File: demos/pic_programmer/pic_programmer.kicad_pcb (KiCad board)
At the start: 2 copper layers, 160 x 99.1 mm, 63 parts, among them J1 DB9-FEMAL, P1 CONN_2, P101 CONN_1, P102 CONN_1, P103 CONN_1, P104 CONN_1, P105 CONN_1, P106 CONN_1, P2 SUPP28, P3 SUPP40, Q1 BC237, Q2 BC307, Q3 BC307, U1 24Cxx, U2 74HC125, U3 7805, U4 LT1373, U5 PIC_18_PINS, U6 PIC_8_PINS

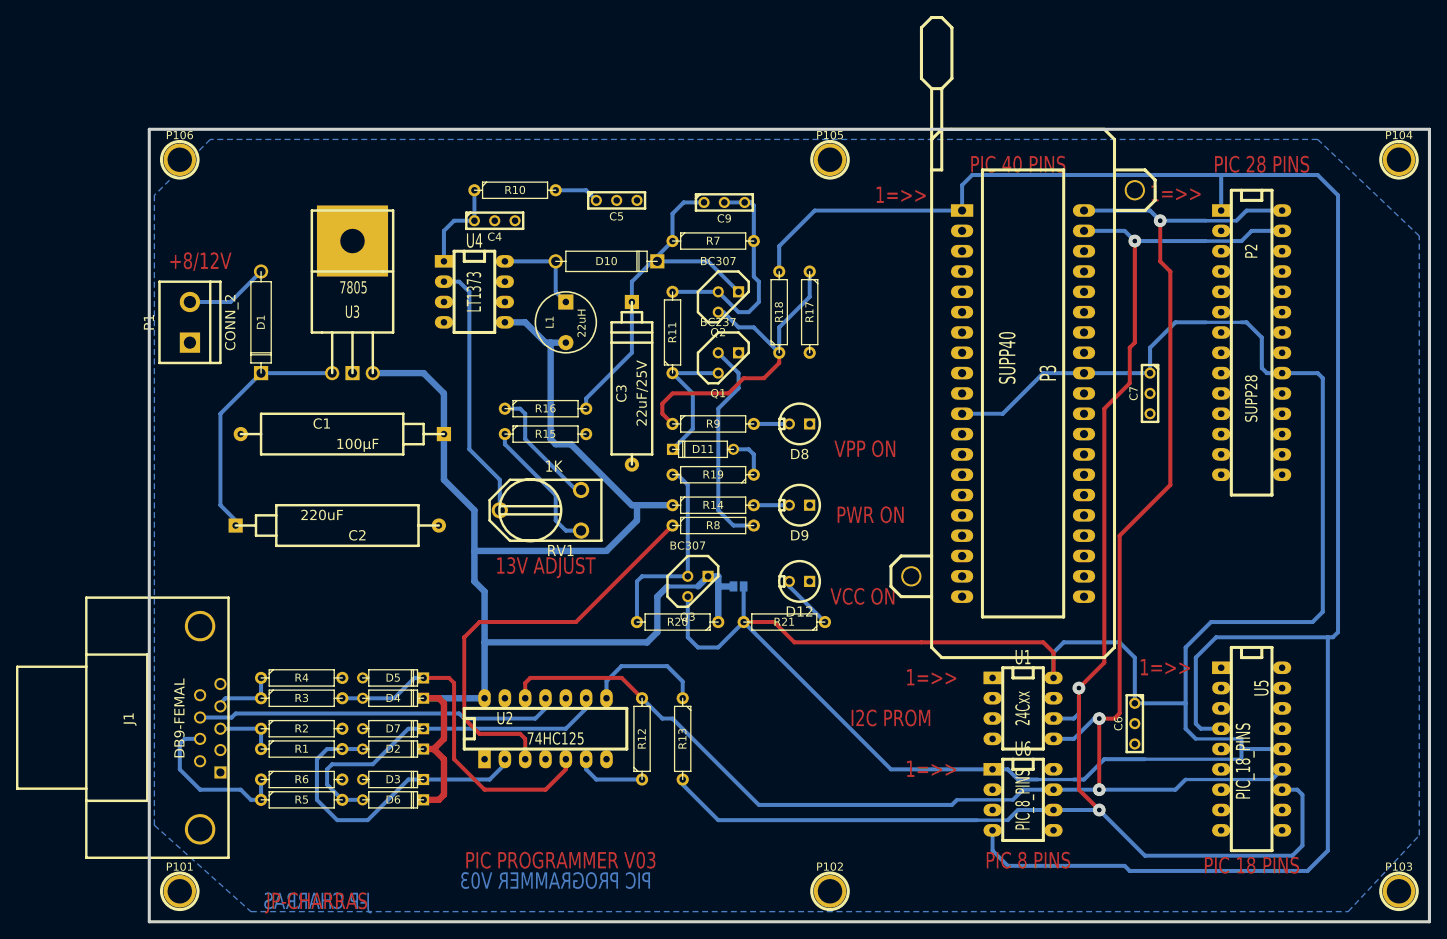
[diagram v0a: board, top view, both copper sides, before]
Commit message: Update demo to use latest libraries.
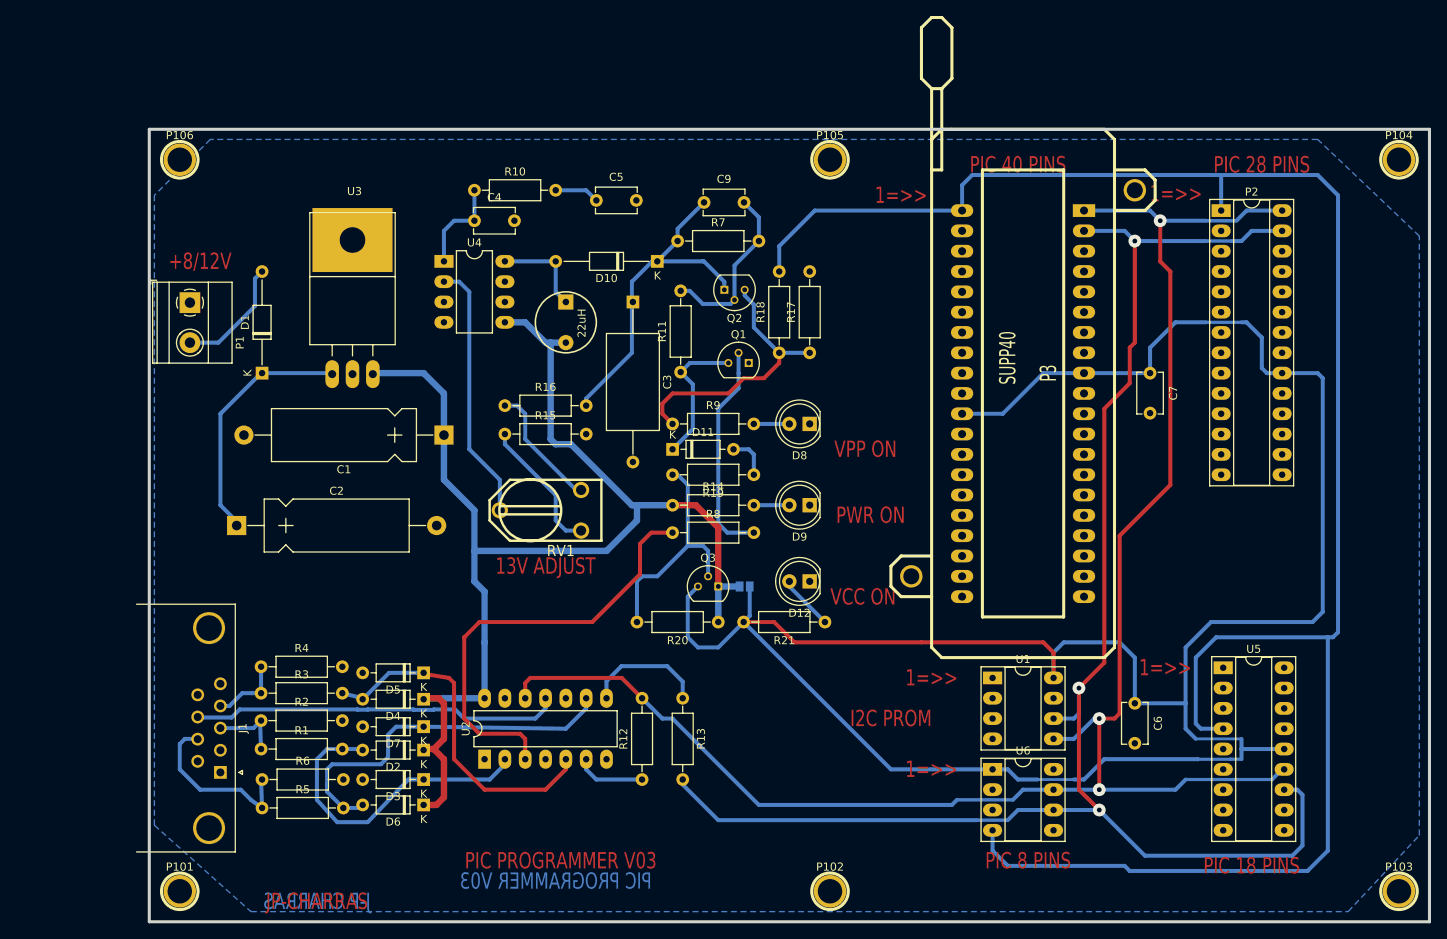
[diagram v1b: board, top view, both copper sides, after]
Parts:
- C1, C2: footprint Discret:CP10 -> Capacitors_THT:CP_Axial_L18.0mm_D6.5mm_P25.00mm_Horizontal
- C3: footprint Discret:CP8 -> Capacitors_THT:C_Axial_L12.0mm_D6.5mm_P20.00mm_Horizontal
- C4, C5, C6, C7, C9: footprint Discret:C1-1 -> C_Disc_D5.1mm_W3.2mm_P5.00mm
- D1, D10: footprint Discret:D5 -> Diode_THT:D_DO-35_SOD27_P12.70mm_Horizontal
- D11, D2, D3, D4, D5, D6, D7: footprint Discret:D3 -> Diode_THT:D_DO-35_SOD27_P7.62mm_Horizontal
- D12, D8, D9: footprint Discret:LEDV -> footprints:LED_D5.0mm
- J1: footprint connect:DB9FC -> Connector_Dsub:DSUB-9_Female_Horizontal_P2.77x2.84mm_EdgePinOffset7.70mm_Housed_MountingHolesOffset9.12mm
- L1: footprint inductors:INDUCTOR_V -> footprints:INDUCTOR_V
- P1: footprint connect:bornier2 -> TerminalBlock_Phoenix:TerminalBlock_Phoenix_MKDS-1,5-2_1x02_P5.00mm_Horizontal
- P2: footprint dip_sockets:DIP-28__300_ELL -> Package_DIP:DIP-28_W7.62mm_Socket_LongPads
- P3: footprint sockets:40tex-Ell600 -> 40tex-Ell600
- Q1, Q2, Q3: footprint Discret:TO92 -> footprints:TO-92_BC237_307
- R1, R10, R11, R12, R13, R14, R15, R16, R17, R18, R19, R2, R20, R21, R3, R4, R5, R6, R7, R8, R9: footprint Discret:R4 -> Resistors_THT:R_Axial_DIN0207_L6.3mm_D2.5mm_P10.16mm_Horizontal
- RV1: footprint Discret:RV2X4 -> footprints:RV2X4
- U1, U6: footprint dip_sockets:DIP-8__300_ELL -> Package_DIP:DIP-8_W7.62mm_Socket_LongPads
- U2: footprint dip_sockets:DIP-14__300_ELL -> Package_DIP:DIP-14_W7.62mm_LongPads
- U3: footprint Discret:LM78XX -> footprints:TO-220_LM78xx
- U4: footprint dip_sockets:DIP-8__300_ELL -> Package_DIP:DIP-8_W7.62mm_LongPads
- U5: footprint dip_sockets:DIP-18__300_ELL -> Package_DIP:DIP-18_W7.62mm_Socket_LongPads
- moved P2 16.9 mm to (207.6, 50.8), turned to 0 degrees
- moved C1 12.7 mm to (110.5, 78.9)
- moved C2 12.6 mm to (84.6, 90.2)
- moved U5 10.8 mm to (207.9, 108.0), turned to 0 degrees
- moved C3 10.2 mm to (134.1, 62.2)
- moved U2 8.52 mm to (115.6, 119.4), turned to 90 degrees
- moved D1 6.35 mm to (87.8, 71.1), turned to 90 degrees
- moved D10 6.35 mm to (137.2, 57.1), turned to 180 degrees
- moved J1 5.61 mm to (82.5, 121.0), turned to 270 degrees
- moved U1 5.39 mm to (179.1, 109.2), turned to 0 degrees
- moved U4 5.39 mm to (110.5, 57.1), turned to 0 degrees
- moved U6 5.39 mm to (179.1, 120.7), turned to 0 degrees
- moved R4 5.27 mm to (87.6, 107.8)
- moved R2 5.18 mm to (87.6, 114.6)
- moved R8 5.16 mm to (139.1, 91.1)
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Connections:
- J1 pad 1: (no net) -> Net-(J1-Pad1)
- J1 pad 2: (no net) -> Net-(J1-Pad2)
- J1 pad 6: (no net) -> Net-(J1-Pad6)
- J1 pad 9: (no net) -> Net-(J1-Pad9)
- P101 pad 1: (no net) -> Net-(P101-Pad1)
- P102 pad 1: (no net) -> Net-(P102-Pad1)
- P103 pad 1: (no net) -> Net-(P103-Pad1)
- P104 pad 1: (no net) -> Net-(P104-Pad1)
- P105 pad 1: (no net) -> Net-(P105-Pad1)
- P106 pad 1: (no net) -> Net-(P106-Pad1)
- P2 pad 10: (no net) -> Net-(P2-Pad10)
- P2 pad 11: (no net) -> Net-(P2-Pad11)
- P2 pad 12: (no net) -> Net-(P2-Pad12)
- P2 pad 13: (no net) -> Net-(P2-Pad13)
- P2 pad 14: (no net) -> Net-(P2-Pad14)
- P2 pad 15: (no net) -> Net-(P2-Pad15)
- P2 pad 16: (no net) -> Net-(P2-Pad16)
- P2 pad 17: (no net) -> Net-(P2-Pad17)
- P2 pad 18: (no net) -> Net-(P2-Pad18)
- P2 pad 2: (no net) -> Net-(P2-Pad2)
- P2 pad 21: (no net) -> Net-(P2-Pad21)
- P2 pad 22: (no net) -> Net-(P2-Pad22)
- P2 pad 23: (no net) -> Net-(P2-Pad23)
- P2 pad 24: (no net) -> Net-(P2-Pad24)
- P2 pad 25: (no net) -> Net-(P2-Pad25)
- P2 pad 26: (no net) -> Net-(P2-Pad26)
- P2 pad 3: (no net) -> Net-(P2-Pad3)
- P2 pad 4: (no net) -> Net-(P2-Pad4)
- P2 pad 5: (no net) -> Net-(P2-Pad5)
- P2 pad 6: (no net) -> Net-(P2-Pad6)
- P2 pad 7: (no net) -> Net-(P2-Pad7)
- P2 pad 9: (no net) -> Net-(P2-Pad9)
- P3 pad 10: (no net) -> Net-(P3-Pad10)
- P3 pad 13: (no net) -> Net-(P3-Pad13)
- P3 pad 14: (no net) -> Net-(P3-Pad14)
- P3 pad 15: (no net) -> Net-(P3-Pad15)
- P3 pad 16: (no net) -> Net-(P3-Pad16)
- P3 pad 17: (no net) -> Net-(P3-Pad17)
- P3 pad 18: (no net) -> Net-(P3-Pad18)
- P3 pad 19: (no net) -> Net-(P3-Pad19)
- P3 pad 2: (no net) -> Net-(P3-Pad2)
- P3 pad 20: (no net) -> Net-(P3-Pad20)
- P3 pad 21: (no net) -> Net-(P3-Pad21)
- P3 pad 22: (no net) -> Net-(P3-Pad22)
- P3 pad 23: (no net) -> Net-(P3-Pad23)
- P3 pad 24: (no net) -> Net-(P3-Pad24)
- P3 pad 25: (no net) -> Net-(P3-Pad25)
- P3 pad 26: (no net) -> Net-(P3-Pad26)
- P3 pad 27: (no net) -> Net-(P3-Pad27)
- P3 pad 28: (no net) -> Net-(P3-Pad28)
- P3 pad 29: (no net) -> Net-(P3-Pad29)
- P3 pad 3: (no net) -> Net-(P3-Pad3)
- P3 pad 30: (no net) -> Net-(P3-Pad30)
- P3 pad 33: (no net) -> Net-(P3-Pad33)
- P3 pad 34: (no net) -> Net-(P3-Pad34)
- P3 pad 35: (no net) -> Net-(P3-Pad35)
- P3 pad 36: (no net) -> Net-(P3-Pad36)
- P3 pad 37: (no net) -> Net-(P3-Pad37)
- P3 pad 38: (no net) -> Net-(P3-Pad38)
- P3 pad 4: (no net) -> Net-(P3-Pad4)
- P3 pad 5: (no net) -> Net-(P3-Pad5)
- P3 pad 6: (no net) -> Net-(P3-Pad6)
- P3 pad 7: (no net) -> Net-(P3-Pad7)
- P3 pad 9: (no net) -> Net-(P3-Pad9)
- U1 pad 7: (no net) -> Net-(U1-Pad7)
- U4 pad 3: (no net) -> Net-(U4-Pad3)
- U4 pad 4: (no net) -> Net-(U4-Pad4)
- U5 pad 1: (no net) -> Net-(U5-Pad1)
- U5 pad 10: (no net) -> Net-(U5-Pad10)
- U5 pad 11: (no net) -> Net-(U5-Pad11)
- U5 pad 15: (no net) -> Net-(U5-Pad15)
- U5 pad 16: (no net) -> Net-(U5-Pad16)
- U5 pad 17: (no net) -> Net-(U5-Pad17)
- U5 pad 18: (no net) -> Net-(U5-Pad18)
- U5 pad 2: (no net) -> Net-(U5-Pad2)
- U5 pad 3: (no net) -> Net-(U5-Pad3)
- U5 pad 6: (no net) -> Net-(U5-Pad6)
- U5 pad 7: (no net) -> Net-(U5-Pad7)
- U5 pad 8: (no net) -> Net-(U5-Pad8)
- U5 pad 9: (no net) -> Net-(U5-Pad9)
- U6 pad 2: (no net) -> Net-(U6-Pad2)
- U6 pad 3: (no net) -> Net-(U6-Pad3)
- U6 pad 5: (no net) -> Net-(U6-Pad5)
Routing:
- net VCC: track 183.3 -> 162.1 mm
- net Net-(Q2-Pad3): track 42.5 -> 34.5 mm
- net Net-(C9-Pad2): track 28.5 -> 21.8 mm
- net Net-(D1-Pad2): track 10.5 -> 14.7 mm
- net Net-(Q3-Pad2): track 25.6 -> 29.3 mm
- net VPP: track 45.5 -> 42.3 mm
- net Net-(D6-Pad2): track 44.0 -> 46.8 mm
- net /pic_sockets/VCC_PIC: track 290.3 -> 292.4 mm
- net Net-(R8-Pad1): track 53.2 -> 55.1 mm
- net /PC-CLOCK-OUT: track 20.3 -> 21.7 mm
- net /TXD: track 7.62 -> 9.03 mm
- net /DTR: track 8.26 -> 9.04 mm

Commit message: Update demo
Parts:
- C4, C5, C6, C7, C9: footprint C_Disc_D5.1mm_W3.2mm_P5.00mm -> Capacitor_THT:C_Disc_D5.1mm_W3.2mm_P5.00mm
- P3: footprint 40tex-Ell600 -> footprints:40tex-Ell600
- R1, R10, R11, R12, R13, R14, R15, R16, R17, R18, R19, R2, R20, R21, R3, R4, R5, R6, R7, R8, R9: footprint Resistors_THT:R_Axial_DIN0207_L6.3mm_D2.5mm_P10.16mm_Horizontal -> Resistor_THT:R_Axial_DIN0207_L6.3mm_D2.5mm_P10.16mm_Horizontal
- moved P1 2.51 mm to (78.7, 62.3)

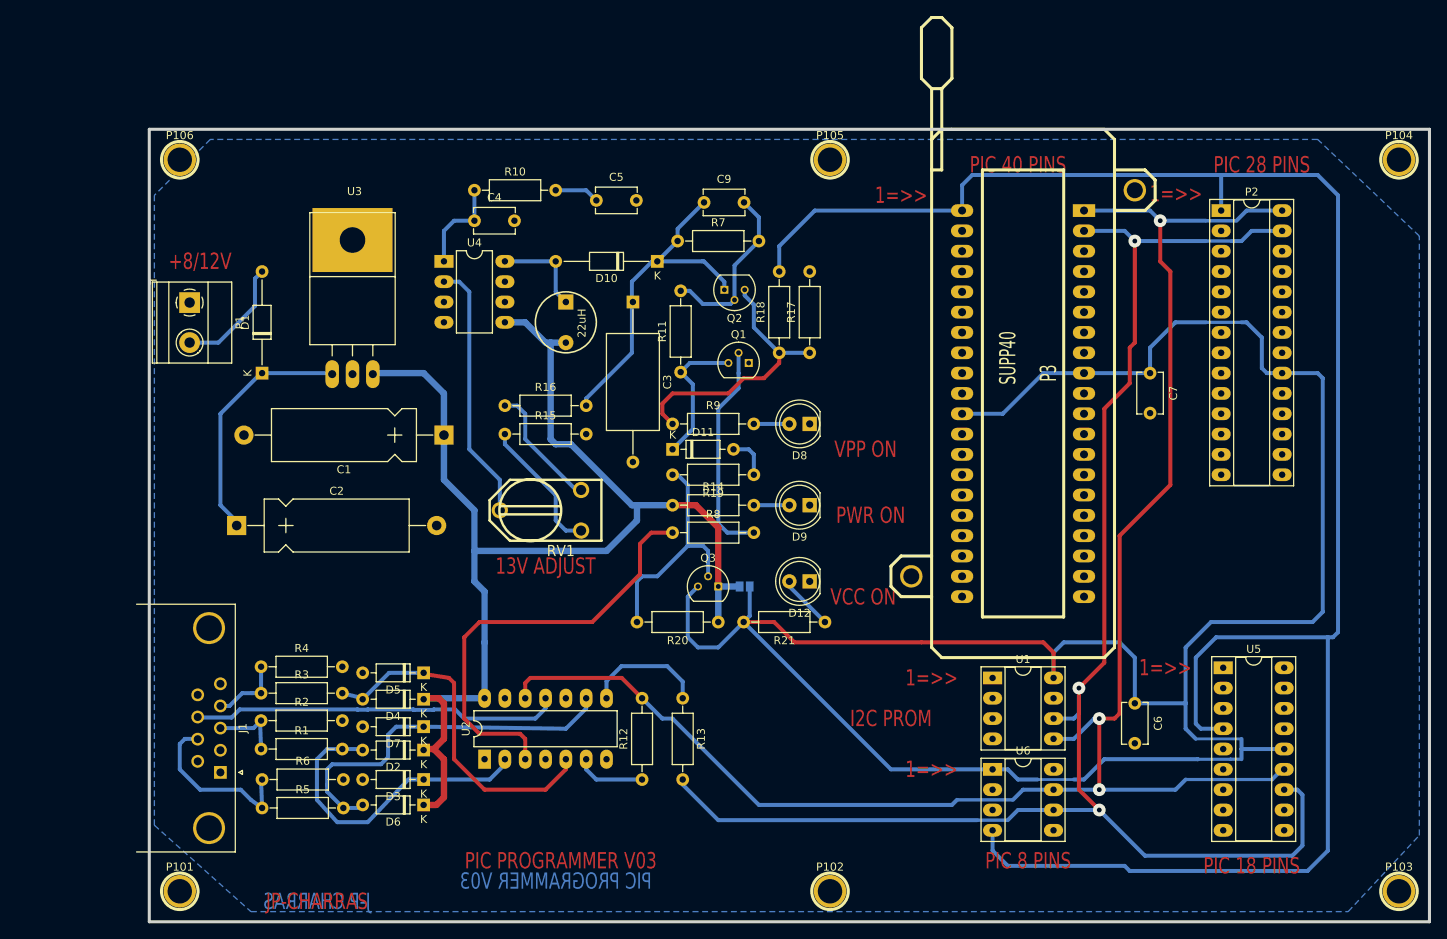
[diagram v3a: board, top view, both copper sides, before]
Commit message: Update demos to use V5 libraries.
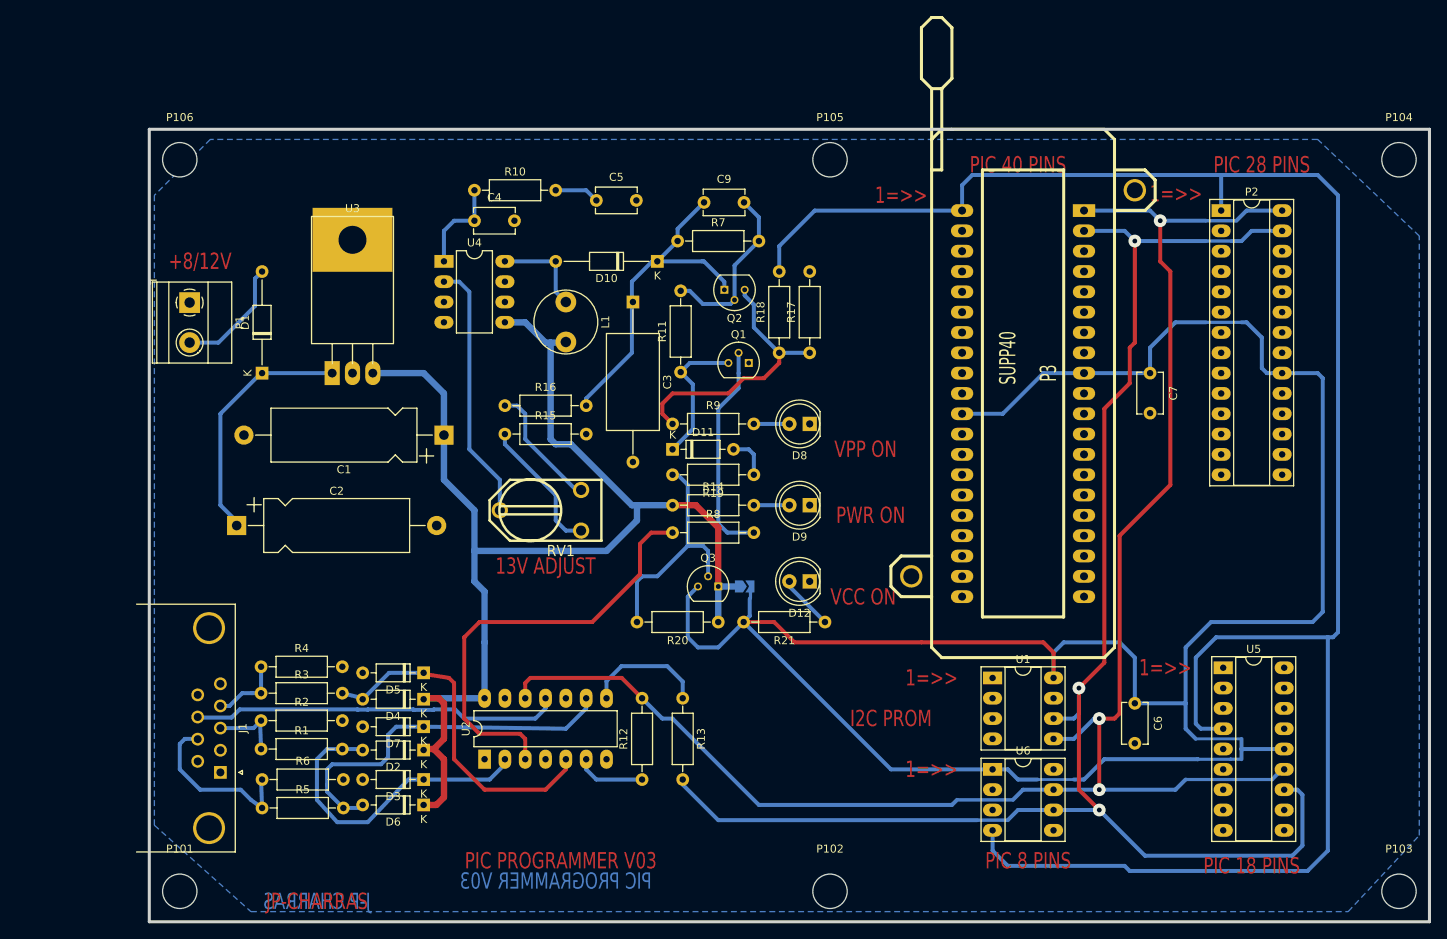
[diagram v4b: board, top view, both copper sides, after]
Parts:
- C1, C2: footprint Capacitors_THT:CP_Axial_L18.0mm_D6.5mm_P25.00mm_Horizontal -> Capacitor_THT:CP_Axial_L18.0mm_D6.5mm_P25.00mm_Horizontal
- D12, D8, D9: footprint footprints:LED_D5.0mm -> LED_THT:LED_D5.0mm
- JP1: footprint connect:GS2 -> Jumper:SolderJumper-2_P1.3mm_Open_TrianglePad1.0x1.5mm
- L1: footprint footprints:INDUCTOR_V -> Inductor_THT:L_Radial_D7.8mm_P5.00mm_Fastron_07HCP
- P101, P102, P103, P104, P105, P106: footprint footprints:1pin-4 -> MountingHole:MountingHole_4.3mm_M4
- U3: footprint footprints:TO-220_LM78xx -> Package_TO_SOT_THT:TO-220-3_Horizontal_TabDown
- moved U3 2.54 mm to (96.5, 71.1)
- moved L1 2.54 mm to (125.7, 62.2)
- turned JP1 to 0 degrees
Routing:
- net /pic_sockets/VCC_PIC: track 292.4 -> 293.3 mm
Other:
- rule trace_min: 0.254 -> 0.25
- rule via_min_drill: 0.508 -> 0.5
- rule via_min_size: 0.889 -> 0.9

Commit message: Update demos.
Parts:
- moved J1 0.83 mm to (82.6, 120.2)
